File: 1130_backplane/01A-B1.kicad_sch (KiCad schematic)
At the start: 86 parts

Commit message: Finish page KT301-KT331
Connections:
- net -PROG_START_KEY_1: now reaches J172.a3 (Pin_a3)
- net +POWER_ON_RESET: now reaches J172.a8 (Pin_a8)
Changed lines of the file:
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@@
+    (effects (font (size 1.27 1.27)) (justify right bottom))
+  )
+  (label "+POWER_ON_RESET" (at 795.02 312.42 180)
     (effects (font (size 1.27 1.27)) (justify right bottom))
   )
@@
     (effects (font (size 1.27 1.27)) (justify right bottom))
   )
+  (label "-PROG_START_KEY_1" (at 795.02 299.72 180)
+    (effects (font (size 1.27 1.27)) (justify right bottom))
+  )

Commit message: Finish page KU201-KU211
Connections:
- net +3V: no longer J171.b2 (Pin_b2)
- net +6V: no longer J171.a10 (Pin_a10)
- net -3V: no longer J171.a5 (Pin_a5)
- net +CPU_STOP_LATCH: now reaches J172.b9 (Pin_b9)
- net +CPU_STOP_LATCH: now also J90.b8 (Pin_b8)
- net +T6_PWR_1: now reaches J171.a11 (Pin_a11)
- net +T4_PWR: now reaches J171.a12 (Pin_a12)
- net +X4_PWR: now reaches J171.b11 (Pin_b11)
- net -X6_PWR: now reaches J171.b12 (Pin_b12)
- new net +OSC_A_PWR: J171.a10 (Pin_a10)
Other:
- note added: "CABL 01A-B1A6"
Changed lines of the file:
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@@
     (stroke (width 0) (type default) (color 0 0 0 0))
   )
-  (wire (pts (xy 807.72 259.08) (xy 815.34 259.08))
-    (stroke (width 0) (type default) (color 0 0 0 0))
-  )
   (wire (pts (xy 469.9 165.1) (xy 477.52 165.1))
     (stroke (width 0) (type default) (color 0 0 0 0))
@@
     (stroke (width 0) (type default) (color 0 0 0 0))
   )
-  (wire (pts (xy 787.4 266.7) (xy 795.02 266.7))
-    (stroke (width 0) (type default) (color 0 0 0 0))
-  )
   (polyline (pts (xy 325.12 29.21) (xy 325.12 27.94))
     (stroke (width 0) (type solid) (color 0 0 0 0))
@@
     (stroke (width 0) (type default) (color 0 0 0 0))
   )
-  (wire (pts (xy 787.4 279.4) (xy 795.02 279.4))
-    (stroke (width 0) (type default) (color 0 0 0 0))
-  )
   (wire (pts (xy 88.9 304.8) (xy 96.52 304.8))
     (stroke (width 0) (type default) (color 0 0 0 0))
@@
     (effects (font (size 5 5) (thickness 1) bold) (justify left bottom))
   )
+  (text "CABL 01A-B1A6" (at 793.75 254 0)
+    (effects (font (size 1.27 1.27)) (justify left bottom))
+  )
   (text "D" (at 34.29 40.64 0)
     (effects (font (size 1.27 1.27)) (justify left bottom))
@@
     (effects (font (size 1.27 1.27)) (justify right bottom))
   )
+  (label "+OSC_A_PWR" (at 795.02 279.4 180)
+    (effects (font (size 1.27 1.27)) (justify right bottom))
+  )
   (label "+3V" (at 434.34 220.98 0)
     (effects (font (size 1.27 1.27)) (justify left bottom))
@@
     (effects (font (size 1.27 1.27)) (justify left bottom))
   )
+  (label "+X4_PWR" (at 807.72 281.94 0)
+    (effects (font (size 1.27 1.27)) (justify left bottom))
+  )
   (label "+6V" (at 596.9 203.2 180)
     (effects (font (size 1.27 1.27)) (justify right bottom))
@@
     (effects (font (size 1.27 1.27)) (justify right bottom))
   )
+  (label "+T6_PWR_1" (at 795.02 281.94 180)
+    (effects (font (size 1.27 1.27)) (justify right bottom))
+  )
   (label "-3V" (at 88.9 228.6 180)
     (effects (font (size 1.27 1.27)) (justify right bottom))
@@
     (effects (font (size 1.27 1.27)) (justify right bottom))
   )
+  (label "-X6_PWR" (at 807.72 284.48 0)
+    (effects (font (size 1.27 1.27)) (justify left bottom))
+  )
   (label "GND" (at 688.34 119.38 0)
     (effects (font (size 1.27 1.27)) (justify left bottom))
@@
     (effects (font (size 1.27 1.27)) (justify left bottom))
   )
-  (label "+6V" (at 787.4 279.4 180)
-    (effects (font (size 1.27 1.27)) (justify right bottom))
-  )
   (label "-3V" (at 279.4 190.5 180)
     (effects (font (size 1.27 1.27)) (justify right bottom))
@@
     (effects (font (size 1.27 1.27)) (justify right bottom))
   )
+  (label "+T4_PWR" (at 795.02 284.48 180)
+    (effects (font (size 1.27 1.27)) (justify right bottom))
+  )
   (label "+3V" (at 323.85 53.34 180)
     (effects (font (size 1.27 1.27)) (justify right bottom))
@@
     (effects (font (size 1.27 1.27)) (justify right bottom))
   )
+  (label "+CPU_STOP_LATCH" (at 807.72 314.96 0)
+    (effects (font (size 1.27 1.27)) (justify left bottom))
+  )
   (label "+3V" (at 180.34 297.18 0)
     (effects (font (size 1.27 1.27)) (justify left bottom))
@@
     (effects (font (size 1.27 1.27)) (justify right bottom))
   )
-  (label "+3V" (at 815.34 259.08 0)
-    (effects (font (size 1.27 1.27)) (justify left bottom))
-  )
   (label "+3V" (at 370.84 106.68 0)
     (effects (font (size 1.27 1.27)) (justify left bottom))
@@
     (effects (font (size 1.27 1.27)) (justify right bottom))
   )
+  (label "+CPU_STOP_LATCH" (at 45.72 236.22 0)
+    (effects (font (size 1.27 1.27)) (justify left bottom))
+  )
   (label "-3V" (at 660.4 152.4 180)
     (effects (font (size 1.27 1.27)) (justify right bottom))
@@
     (effects (font (size 1.27 1.27)) (justify right bottom))
   )
-  (label "-3V" (at 787.4 266.7 180)
-    (effects (font (size 1.27 1.27)) (justify right bottom))
-  )

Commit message: Finish page KU301-KU311, minor column label fix.
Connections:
- net -DC_RESET_IAR: now reaches J172.b2 (Pin_b2)
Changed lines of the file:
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@@
     (effects (font (size 1.27 1.27)) (justify left bottom))
   )
-  (text "H" (at 482.6 337.82 0)
+  (text "H" (at 481.33 337.82 0)
     (effects (font (size 5 5) (thickness 1) bold) (justify left bottom))
   )
@@
     (effects (font (size 1.27 1.27)) (justify left bottom))
   )
-  (text "H" (at 482.6 90.17 0)
+  (text "H" (at 481.33 90.17 0)
     (effects (font (size 5 5) (thickness 1) bold) (justify left bottom))
   )
@@
     (effects (font (size 1.27 1.27)) (justify right bottom))
   )
+  (label "-DC_RESET_IAR" (at 807.72 297.18 0)
+    (effects (font (size 1.27 1.27)) (justify left bottom))
+  )
   (label "-3V" (at 279.4 266.7 180)

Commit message: Finish page KW101. Add 48V bus for 01A-C1
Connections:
- net +CPU_RUN: now reaches J172.b6 (Pin_b6)
- net +CPU_RUN: now also J90.b6 (Pin_b6)
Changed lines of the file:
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@@
+    (effects (font (size 1.27 1.27)) (justify left bottom))
+  )
+  (label "+CPU_RUN" (at 45.72 231.14 0)
     (effects (font (size 1.27 1.27)) (justify left bottom))
   )
@@
     (effects (font (size 1.27 1.27)) (justify left bottom))
   )
+  (label "+CPU_RUN" (at 807.72 307.34 0)
+    (effects (font (size 1.27 1.27)) (justify left bottom))
+  )

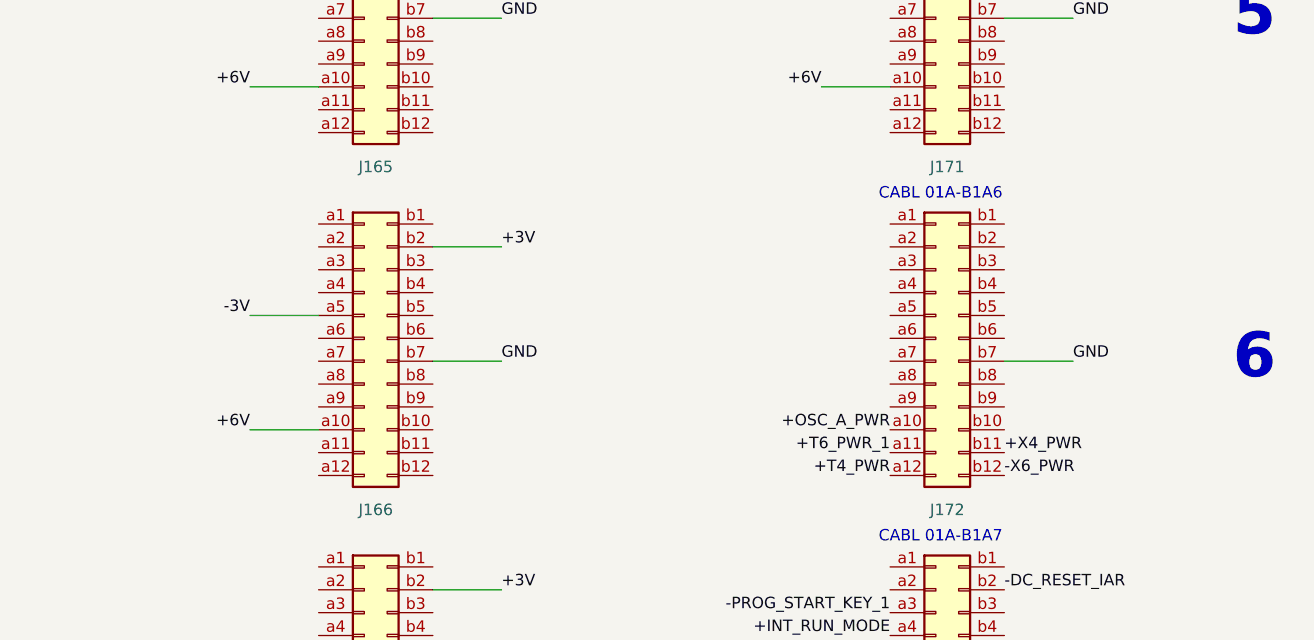
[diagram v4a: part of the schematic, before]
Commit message: Finish page RB301-RB321
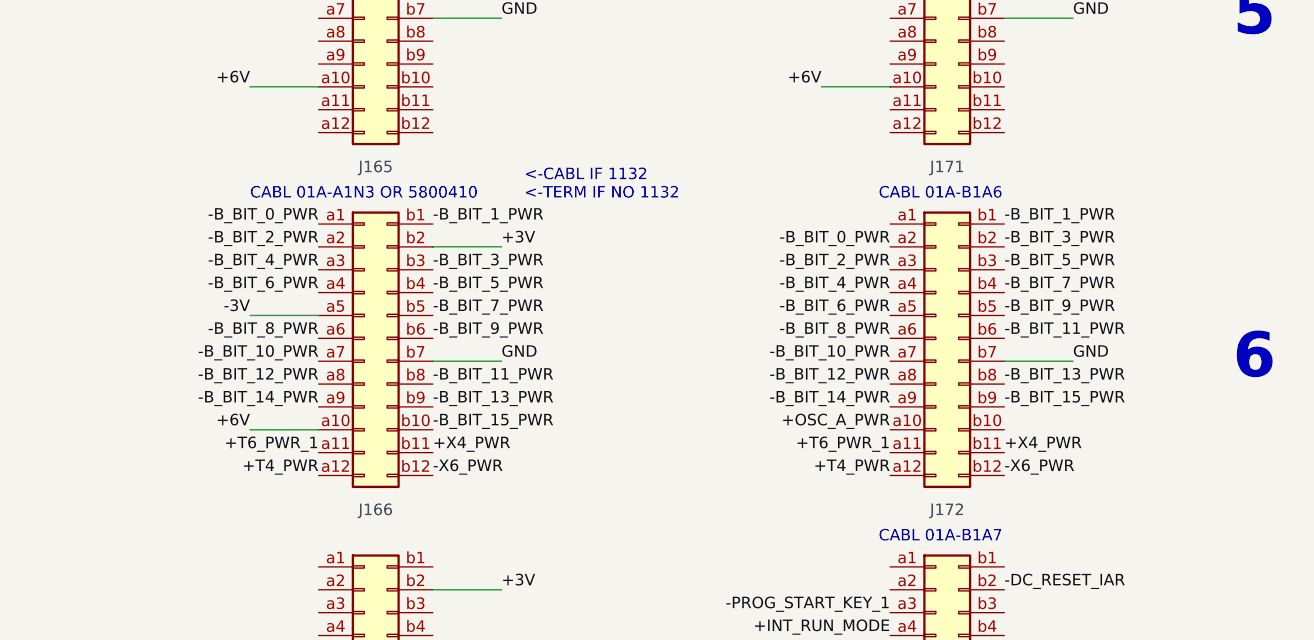
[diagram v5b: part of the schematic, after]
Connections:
- net +T4_PWR: now also J165.a12 (Pin_a12)
- net +T6_PWR_1: now also J165.a11 (Pin_a11)
- net +X4_PWR: now also J165.b11 (Pin_b11)
- net -X6_PWR: now also J165.b12 (Pin_b12)
- net -B_BIT_0_PWR: now reaches J165.a1 (Pin_a1)
- net -B_BIT_0_PWR: now also J171.a2 (Pin_a2)
- net -B_BIT_2_PWR: now reaches J165.a2 (Pin_a2)
- net -B_BIT_2_PWR: now also J171.a3 (Pin_a3)
- net -B_BIT_4_PWR: now reaches J165.a3 (Pin_a3)
- net -B_BIT_4_PWR: now also J171.a4 (Pin_a4)
- net -B_BIT_6_PWR: now reaches J165.a4 (Pin_a4)
- net -B_BIT_6_PWR: now also J171.a5 (Pin_a5)
- net -B_BIT_8_PWR: now reaches J165.a6 (Pin_a6)
- net -B_BIT_8_PWR: now also J171.a6 (Pin_a6)
- net -B_BIT_10_PWR: now reaches J165.a7 (Pin_a7)
- net -B_BIT_10_PWR: now also J171.a7 (Pin_a7)
- net -B_BIT_12_PWR: now reaches J165.a8 (Pin_a8)
- net -B_BIT_12_PWR: now also J171.a8 (Pin_a8)
- net -B_BIT_14_PWR: now reaches J165.a9 (Pin_a9)
- net -B_BIT_14_PWR: now also J171.a9 (Pin_a9)
- net -B_BIT_1_PWR: now reaches J165.b1 (Pin_b1)
- net -B_BIT_1_PWR: now also J171.b1 (Pin_b1)
- net -B_BIT_15_PWR: now reaches J165.b10 (Pin_b10)
- net -B_BIT_15_PWR: now also J171.b9 (Pin_b9)
- net -B_BIT_3_PWR: now reaches J165.b3 (Pin_b3)
- net -B_BIT_3_PWR: now also J171.b2 (Pin_b2)
- net -B_BIT_5_PWR: now reaches J165.b4 (Pin_b4)
- net -B_BIT_5_PWR: now also J171.b3 (Pin_b3)
- net -B_BIT_7_PWR: now reaches J165.b5 (Pin_b5)
- net -B_BIT_7_PWR: now also J171.b4 (Pin_b4)
- net -B_BIT_9_PWR: now reaches J165.b6 (Pin_b6)
- net -B_BIT_9_PWR: now also J171.b5 (Pin_b5)
- net -B_BIT_11_PWR: now reaches J165.b8 (Pin_b8)
- net -B_BIT_11_PWR: now also J171.b6 (Pin_b6)
- net -B_BIT_13_PWR: now reaches J165.b9 (Pin_b9)
- net -B_BIT_13_PWR: now also J171.b8 (Pin_b8)
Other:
- note added: "<-CABL IF 1132 <-TERM IF NO 1132"
- note added: "CABL 01A-A1N3 OR 5800410"
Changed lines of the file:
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@@
     (effects (font (size 5 5) (thickness 1) bold) (justify left bottom))
+  )
+  (text "CABL 01A-A1N3 OR 5800410" (at 723.9 254 0)
+    (effects (font (size 1.27 1.27)) (justify left bottom))
   )
   (text "E" (at 327.66 368.3 0)
@@
     (effects (font (size 1.27 1.27)) (justify left bottom))
   )
+  (text "<-CABL IF 1132\n<-TERM IF NO 1132" (at 754.38 254 0)
+    (effects (font (size 1.27 1.27)) (justify left bottom))
+  )
   (text "L" (at 670.56 90.17 0)
     (effects (font (size 5 5) (thickness 1) bold) (justify left bottom))
@@
     (effects (font (size 1.27 1.27)) (justify left bottom))
   )
+  (label "-B_BIT_9_PWR" (at 807.72 266.7 0)
+    (effects (font (size 1.27 1.27)) (justify left bottom))
+  )
   (label "+6V" (at 88.9 203.2 180)
     (effects (font (size 1.27 1.27)) (justify right bottom))
@@
     (effects (font (size 1.27 1.27)) (justify right bottom))
   )
+  (label "-B_BIT_2_PWR" (at 795.02 261.62 180)
+    (effects (font (size 1.27 1.27)) (justify right bottom))
+  )
   (label "-3V" (at 469.9 228.6 180)
     (effects (font (size 1.27 1.27)) (justify right bottom))
@@
     (effects (font (size 1.27 1.27)) (justify left bottom))
   )
+  (label "-B_BIT_6_PWR" (at 795.02 266.7 180)
+    (effects (font (size 1.27 1.27)) (justify right bottom))
+  )
   (label "+3V" (at 307.34 297.18 0)
     (effects (font (size 1.27 1.27)) (justify left bottom))
@@
     (effects (font (size 1.27 1.27)) (justify right bottom))
   )
+  (label "-B_BIT_12_PWR" (at 795.02 274.32 180)
+    (effects (font (size 1.27 1.27)) (justify right bottom))
+  )
   (label "+6V" (at 660.4 127 180)
     (effects (font (size 1.27 1.27)) (justify right bottom))
   )
+  (label "-B_BIT_3_PWR" (at 744.22 261.62 0)
+    (effects (font (size 1.27 1.27)) (justify left bottom))
+  )
   (label "GND" (at 116.84 271.78 0)
     (effects (font (size 1.27 1.27)) (justify left bottom))
@@
     (effects (font (size 1.27 1.27)) (justify left bottom))
   )
+  (label "-B_BIT_6_PWR" (at 731.52 264.16 180)
+    (effects (font (size 1.27 1.27)) (justify right bottom))
+  )
   (label "+6V" (at 723.9 127 180)
     (effects (font (size 1.27 1.27)) (justify right bottom))
@@
     (effects (font (size 1.27 1.27)) (justify left bottom))
   )
+  (label "-B_BIT_11_PWR" (at 744.22 274.32 0)
+    (effects (font (size 1.27 1.27)) (justify left bottom))
+  )
   (label "+XIO_CONTROL" (at 33.02 236.22 180)
     (effects (font (size 1.27 1.27)) (justify right bottom))
@@
     (effects (font (size 1.27 1.27)) (justify right bottom))
   )
+  (label "-B_BIT_1_PWR" (at 807.72 256.54 0)
+    (effects (font (size 1.27 1.27)) (justify left bottom))
+  )
   (label "+6V" (at 596.9 241.3 180)
     (effects (font (size 1.27 1.27)) (justify right bottom))
@@
     (effects (font (size 1.27 1.27)) (justify left bottom))
   )
+  (label "-X6_PWR" (at 744.22 284.48 0)
+    (effects (font (size 1.27 1.27)) (justify left bottom))
+  )
+  (label "-B_BIT_13_PWR" (at 744.22 276.86 0)
+    (effects (font (size 1.27 1.27)) (justify left bottom))
+  )
   (label "+3V" (at 180.34 182.88 0)
     (effects (font (size 1.27 1.27)) (justify left bottom))
@@
     (effects (font (size 1.27 1.27)) (justify left bottom))
   )
+  (label "-B_BIT_4_PWR" (at 731.52 261.62 180)
+    (effects (font (size 1.27 1.27)) (justify right bottom))
+  )
   (label "-3V" (at 152.4 152.4 180)
     (effects (font (size 1.27 1.27)) (justify right bottom))
   )
+  (label "-B_BIT_15_PWR" (at 744.22 279.4 0)
+    (effects (font (size 1.27 1.27)) (justify left bottom))
+  )
+  (label "-B_BIT_8_PWR" (at 795.02 269.24 180)
+    (effects (font (size 1.27 1.27)) (justify right bottom))
+  )
   (label "-3V" (at 660.4 114.3 180)
     (effects (font (size 1.27 1.27)) (justify right bottom))
@@
     (effects (font (size 1.27 1.27)) (justify right bottom))
   )
+  (label "-B_BIT_10_PWR" (at 795.02 271.78 180)
+    (effects (font (size 1.27 1.27)) (justify right bottom))
+  )
+  (label "-B_BIT_3_PWR" (at 807.72 259.08 0)
+    (effects (font (size 1.27 1.27)) (justify left bottom))
+  )
   (label "+3V" (at 370.84 182.88 0)
     (effects (font (size 1.27 1.27)) (justify left bottom))
@@
     (effects (font (size 1.27 1.27)) (justify right bottom))
   )
+  (label "+T4_PWR" (at 731.52 284.48 180)
+    (effects (font (size 1.27 1.27)) (justify right bottom))
+  )
   (label "-3V" (at 596.9 114.3 180)
     (effects (font (size 1.27 1.27)) (justify right bottom))
@@
     (effects (font (size 1.27 1.27)) (justify left bottom))
   )
+  (label "-B_BIT_10_PWR" (at 731.52 271.78 180)
+    (effects (font (size 1.27 1.27)) (justify right bottom))
+  )
   (label "-3V" (at 723.9 304.8 180)
     (effects (font (size 1.27 1.27)) (justify right bottom))
@@
     (effects (font (size 1.27 1.27)) (justify right bottom))
   )
+  (label "-B_BIT_9_PWR" (at 744.22 269.24 0)
+    (effects (font (size 1.27 1.27)) (justify left bottom))
+  )
   (label "+3V" (at 624.84 182.88 0)
     (effects (font (size 1.27 1.27)) (justify left bottom))
@@
     (effects (font (size 1.27 1.27)) (justify left bottom))
   )
+  (label "+X4_PWR" (at 744.22 281.94 0)
+    (effects (font (size 1.27 1.27)) (justify left bottom))
+  )
   (label "-3V" (at 279.4 304.8 180)
     (effects (font (size 1.27 1.27)) (justify right bottom))
@@
     (effects (font (size 1.27 1.27)) (justify left bottom))
   )
+  (label "-B_BIT_0_PWR" (at 731.52 256.54 180)
+    (effects (font (size 1.27 1.27)) (justify right bottom))
+  )
   (label "+6V" (at 342.9 203.2 180)
     (effects (font (size 1.27 1.27)) (justify right bottom))
@@
     (effects (font (size 1.27 1.27)) (justify left bottom))
   )
+  (label "-B_BIT_4_PWR" (at 795.02 264.16 180)
+    (effects (font (size 1.27 1.27)) (justify right bottom))
+  )
   (label "GND" (at 243.84 271.78 0)
     (effects (font (size 1.27 1.27)) (justify left bottom))
@@
     (effects (font (size 1.27 1.27)) (justify left bottom))
   )
+  (label "-B_BIT_2_PWR" (at 731.52 259.08 180)
+    (effects (font (size 1.27 1.27)) (justify right bottom))
+  )
   (label "+3V" (at 53.34 182.88 0)
     (effects (font (size 1.27 1.27)) (justify left bottom))
@@
     (effects (font (size 1.27 1.27)) (justify right bottom))
   )
+  (label "-B_BIT_0_PWR" (at 795.02 259.08 180)
+    (effects (font (size 1.27 1.27)) (justify right bottom))
+  )
   (label "-3V" (at 723.9 228.6 180)
     (effects (font (size 1.27 1.27)) (justify right bottom))
@@
     (effects (font (size 1.27 1.27)) (justify right bottom))
   )
+  (label "-B_BIT_1_PWR" (at 744.22 256.54 0)
+    (effects (font (size 1.27 1.27)) (justify left bottom))
+  )
   (label "+6V" (at 723.9 241.3 180)
     (effects (font (size 1.27 1.27)) (justify right bottom))
   )
+  (label "-B_BIT_14_PWR" (at 795.02 276.86 180)
+    (effects (font (size 1.27 1.27)) (justify right bottom))
+  )
   (label "+3V" (at 751.84 182.88 0)
     (effects (font (size 1.27 1.27)) (justify left bottom))
@@
     (effects (font (size 1.27 1.27)) (justify left bottom))
   )
+  (label "-B_BIT_13_PWR" (at 807.72 274.32 0)
+    (effects (font (size 1.27 1.27)) (justify left bottom))
+  )
+  (label "+T6_PWR_1" (at 731.52 281.94 180)
+    (effects (font (size 1.27 1.27)) (justify right bottom))
+  )
   (label "-IO_BIT_6" (at 374.65 63.5 270)
     (effects (font (size 1.27 1.27)) (justify right bottom))
   )
+  (label "-B_BIT_7_PWR" (at 744.22 266.7 0)
+    (effects (font (size 1.27 1.27)) (justify left bottom))
+  )
   (label "+XIO_READ" (at 392.43 63.5 270)
     (effects (font (size 1.27 1.27)) (justify right bottom))
@@
     (effects (font (size 1.27 1.27)) (justify right bottom))
   )
+  (label "-B_BIT_12_PWR" (at 731.52 274.32 180)
+    (effects (font (size 1.27 1.27)) (justify right bottom))
+  )
   (label "+6V" (at 723.9 203.2 180)
     (effects (font (size 1.27 1.27)) (justify right bottom))
   )
+  (label "-B_BIT_11_PWR" (at 807.72 269.24 0)
+    (effects (font (size 1.27 1.27)) (justify left bottom))
+  )
   (label "+3V" (at 497.84 259.08 0)
     (effects (font (size 1.27 1.27)) (justify left bottom))
@@
     (effects (font (size 1.27 1.27)) (justify right bottom))
   )
+  (label "-B_BIT_7_PWR" (at 807.72 264.16 0)
+    (effects (font (size 1.27 1.27)) (justify left bottom))
+  )
   (label "-3V" (at 596.9 190.5 180)
     (effects (font (size 1.27 1.27)) (justify right bottom))
@@
     (effects (font (size 1.27 1.27)) (justify left bottom))
   )
+  (label "-B_BIT_15_PWR" (at 807.72 276.86 0)
+    (effects (font (size 1.27 1.27)) (justify left bottom))
+  )
   (label "+6V" (at 152.4 165.1 180)
     (effects (font (size 1.27 1.27)) (justify right bottom))
@@
     (effects (font (size 1.27 1.27)) (justify right bottom))
   )
+  (label "-B_BIT_8_PWR" (at 731.52 269.24 180)
+    (effects (font (size 1.27 1.27)) (justify right bottom))
+  )
   (label "-3V" (at 787.4 114.3 180)
     (effects (font (size 1.27 1.27)) (justify right bottom))
@@
     (effects (font (size 1.27 1.27)) (justify right bottom))
   )
+  (label "-B_BIT_5_PWR" (at 807.72 261.62 0)
+    (effects (font (size 1.27 1.27)) (justify left bottom))
+  )
   (label "+6V" (at 406.4 165.1 180)
     (effects (font (size 1.27 1.27)) (justify right bottom))
@@
     (effects (font (size 1.27 1.27)) (justify right bottom))
   )
+  (label "-B_BIT_14_PWR" (at 731.52 276.86 180)
+    (effects (font (size 1.27 1.27)) (justify right bottom))
+  )
   (label "+3V" (at 624.84 297.18 0)
     (effects (font (size 1.27 1.27)) (justify left bottom))
@@
     (effects (font (size 1.27 1.27)) (justify left bottom))
   )
+  (label "-B_BIT_5_PWR" (at 744.22 264.16 0)
+    (effects (font (size 1.27 1.27)) (justify left bottom))
+  )
